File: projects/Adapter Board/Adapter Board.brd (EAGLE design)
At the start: 45 x 26 mm, 39 parts

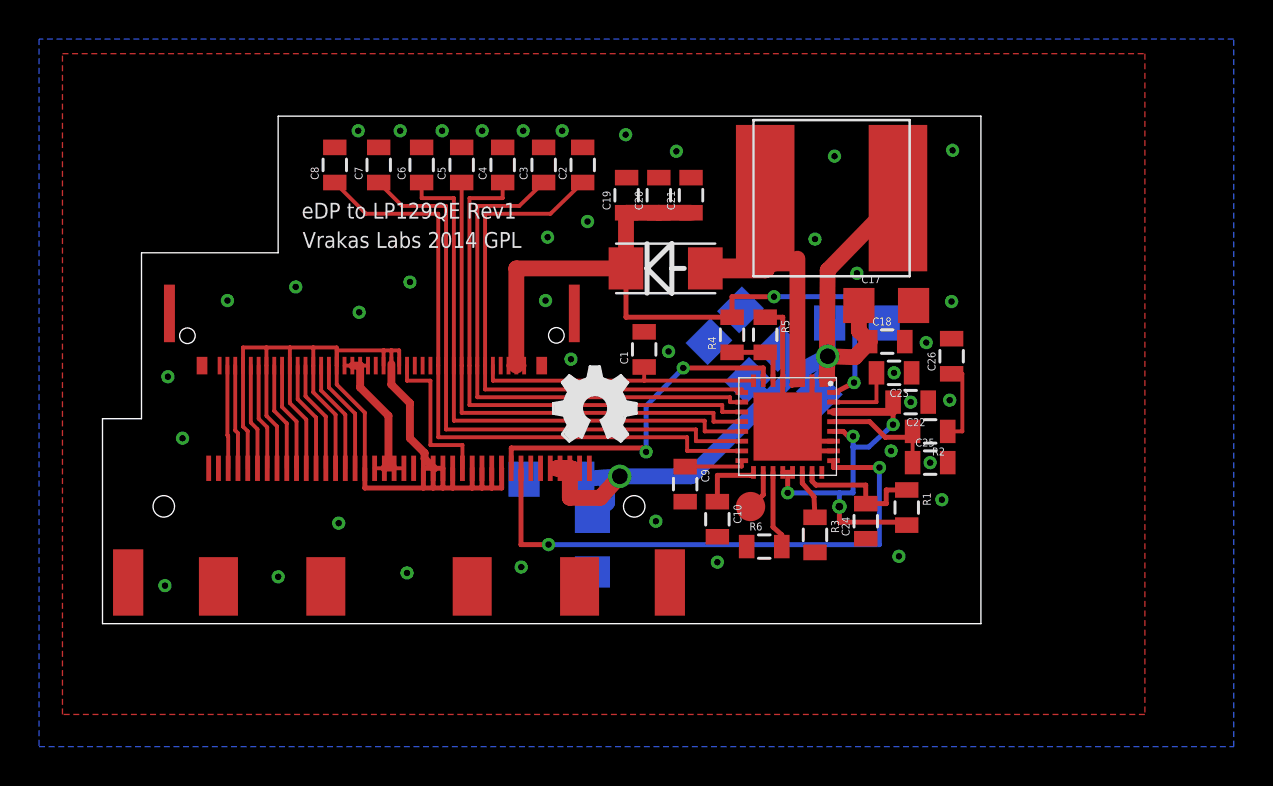
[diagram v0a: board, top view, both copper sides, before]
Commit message: Rev.2 Commit
Joined common pads, removed orphaned pads, aligned passive 0805s. More
room to solder QFN. Full rectangular board.
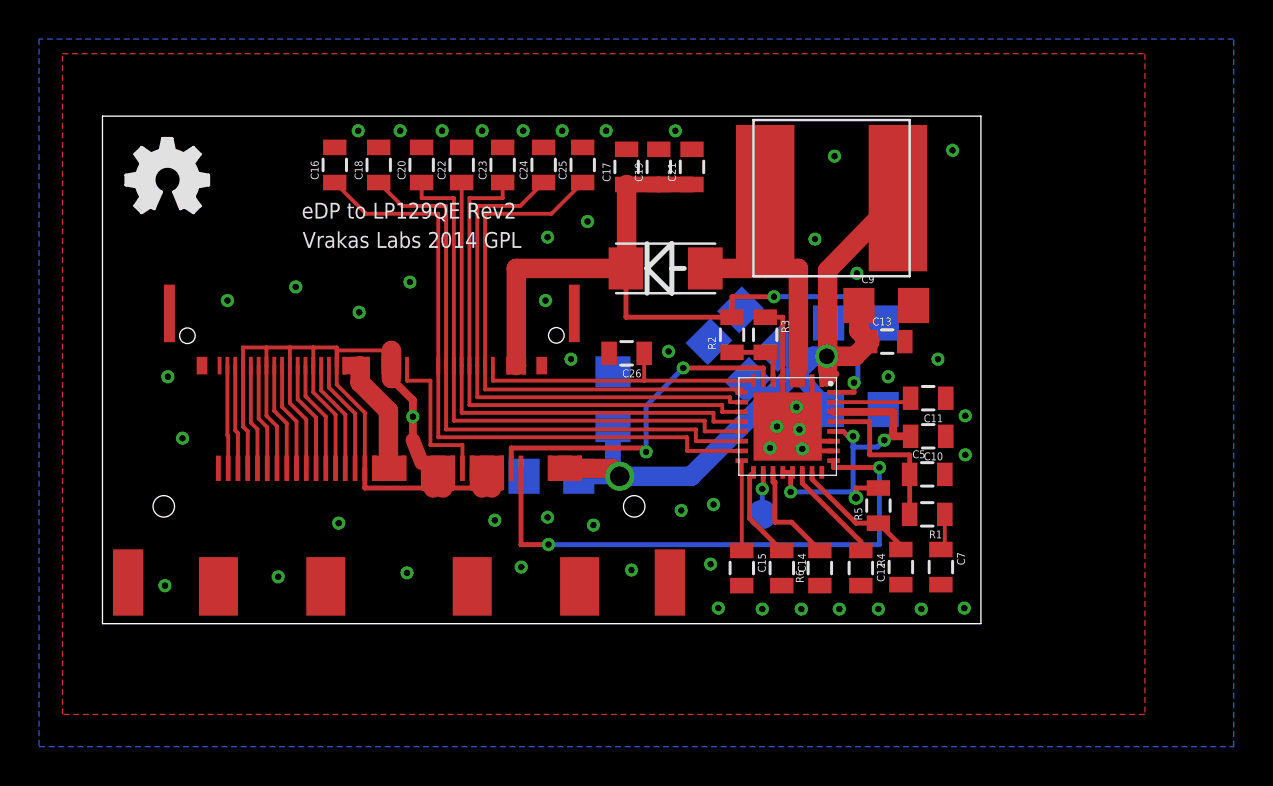
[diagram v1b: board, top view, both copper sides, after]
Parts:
- C1, C2, C3, C4, C6, C8, C9: value 220pF -> 10uF; device SparkFun-Passives:0805 -> SparkFun-Capacitors:1206
- C10: value 220pF -> 2.2uF; device SparkFun-Passives:0805 -> SparkFun-Capacitors:0805
- C11, C12: value 10uF -> 2.2uF; device SparkFun-Capacitors:1206 -> SparkFun-Capacitors:0805
- C13: value 10uF -> 0.1uF; device SparkFun-Capacitors:1206 -> SparkFun-Capacitors:0805
- C14, C15, C16: value 10uF -> 220pF; device SparkFun-Capacitors:1206 -> SparkFun-Passives:0805
- C17: value 10uF -> 4.7uF; device SparkFun-Capacitors:1206 -> SparkFun-Capacitors:0805
- C18: value 0.1uF -> 220pF; device SparkFun-Capacitors:0805 -> SparkFun-Passives:0805
- C20: value 4.7uF -> 220pF; device SparkFun-Capacitors:0805 -> SparkFun-Passives:0805
- C22, C23, C24: value 2.2uF -> 220pF; device SparkFun-Capacitors:0805 -> SparkFun-Passives:0805
- C25: value 100pF -> 220pF; device SparkFun-Capacitors:0805 -> SparkFun-Passives:0805
- C26: value 2700pF -> 220pF; device SparkFun-Capacitors:0805 -> SparkFun-Passives:0805
- C5: value 220pF -> 100pF; device SparkFun-Passives:0805 -> SparkFun-Capacitors:0805
- C7: value 220pF -> 2700pF; device SparkFun-Passives:0805 -> SparkFun-Capacitors:0805
- R1: value 1K -> 5.6K
- R2: value 5.6K -> 150K
- R3: value 66.5K -> 20K
- R4: value 150K -> 66.5K
- R5: value 20K -> 1K
- moved C7 35.4 mm to (43.0, 2.90), turned to 270 degrees
- moved C5 28.6 mm to (42.2, 7.65), turned to 0 degrees
- moved C16 27.9 mm to (11.9, 23.5), flipped to the top, turned to 90 degrees
- moved C8 27.9 mm to (38.6, 15.4), flipped to the bottom, turned to 180 degrees
- moved C18 27.6 mm to (14.2, 23.5), turned to 90 degrees
- moved C22 26.0 mm to (18.4, 23.5), turned to 90 degrees
- moved U$5 24.8 mm to (1.20, 21.1)
- moved C24 24.6 mm to (22.6, 23.5)
- moved C25 23.4 mm to (24.6, 23.5), turned to 90 degrees
- moved C23 22.7 mm to (20.5, 23.5), turned to 90 degrees
- moved C3 20.3 mm to (38.6, 11.0), flipped to the bottom, turned to 180 degrees
- moved C26 16.7 mm to (26.9, 13.8), turned to 180 degrees
- moved C4 16.1 mm to (23.0, 7.55), flipped to the bottom, turned to 0 degrees
- moved C6 15.5 mm to (26.1, 11.5), flipped to the bottom
- moved C17 15.1 mm to (26.9, 23.4), turned to 90 degrees
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- renumbered DIOD-S to D1, U$1 to F1, U$2 to F2, U$3 to U1, U$4 to I1
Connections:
- net BKLT-VCC: now also C1.1, C2.1, C3.1, C4.1, C6.1, C8.1, C9.1; no longer C11.1, C12.1, C14.1, C15.1, C16.1, C17.1, C18.1
- net BL-ANODE: now also C17.1, R2.2; no longer C20.1, R4.2
- net BL0: now also C26.1; no longer C1.1
- net BL1: now also C25.1; no longer C2.1
- net BL2: now also C24.1; no longer C3.1
- net BL3: now also C23.1; no longer C4.1
- net BL4: now also C22.1; no longer C5.1
- net BL5: now also C20.1; no longer C6.1
- net BL6: now also C18.1; no longer C7.1
- net BL7: now also C16.1; no longer C8.1
- net BL8: now also C15.1; no longer C9.1
- net BL9: now also C14.1; no longer C10.1
- net GND: now also C10.1, C11.1, C12.1, C22.2, C23.2, C24.2, R3.1, R4.2; no longer C10.2, C11.2, C12.2, C22.1, C23.1, C24.1, R3.2, R5.1
- net N$1: now also C5.1, R1.2; no longer C25.1, R2.2
- net N$10: now also C12.2, R5.1; no longer C24.2, R1.1
- net N$13: now also C7.1, R1.1; no longer C26.1, R2.1
- net N$16: now also R2.1, R3.2; no longer R4.1, R5.2
- net N$17: now also R4.1; no longer R3.1
- net N$4: now also C11.2; no longer C23.2
- net VDC1: now also C10.2, R5.2; no longer C22.2, R1.2
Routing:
- net N$17: track 2.52 -> 5.24 mm
- net VDC1: track 20.9 -> 18.2 mm
- net N$1: track 6.14 -> 8.65 mm
- net N$13: track 4.25 -> 2.00 mm
- net BL-ANODE: track 38.4 -> 40.6 mm
- net N$20: track 4.00 -> 5.55 mm
- net BL9: track 3.26 -> 4.77 mm
- net BL8: track 3.20 -> 4.60 mm
- net SWA/B: track 16.3 -> 15.5 mm
- net BL0: track 14.8 -> 15.5 mm
- net N$10: track 7.03 -> 6.51 mm
- net GND: track 82.9 -> 83.4 mm, vias 39 -> 52
- net N$18: track 2.03 -> 2.20 mm, vias 0 -> 1
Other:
- outline, holes or cut-outs redrawn
- board text added: "eDP to LP129QE Rev2"
- board text removed: "eDP to LP129QE Rev1"
